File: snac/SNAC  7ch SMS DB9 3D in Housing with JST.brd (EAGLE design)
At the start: 61.2 x 64.1 mm, 51 parts, among them IC1 4030D, IC3 4030D, Q1 BSS138, Q2 BSS138, Q3 BSS138, Q4 BSS138, Q5 BSS138, Q6 BSS138, Q7 BSS138, Q8 BSS138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

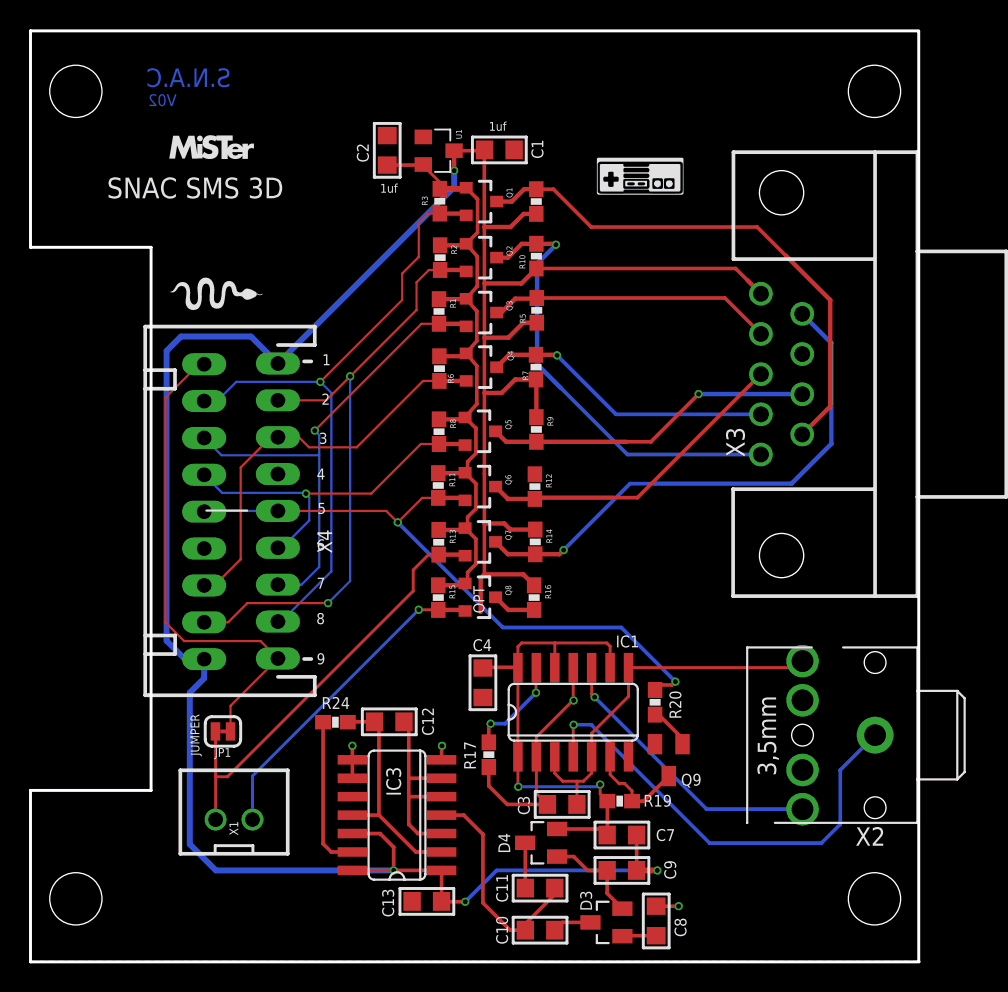
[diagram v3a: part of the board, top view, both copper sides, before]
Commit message: Updated PCB images and README
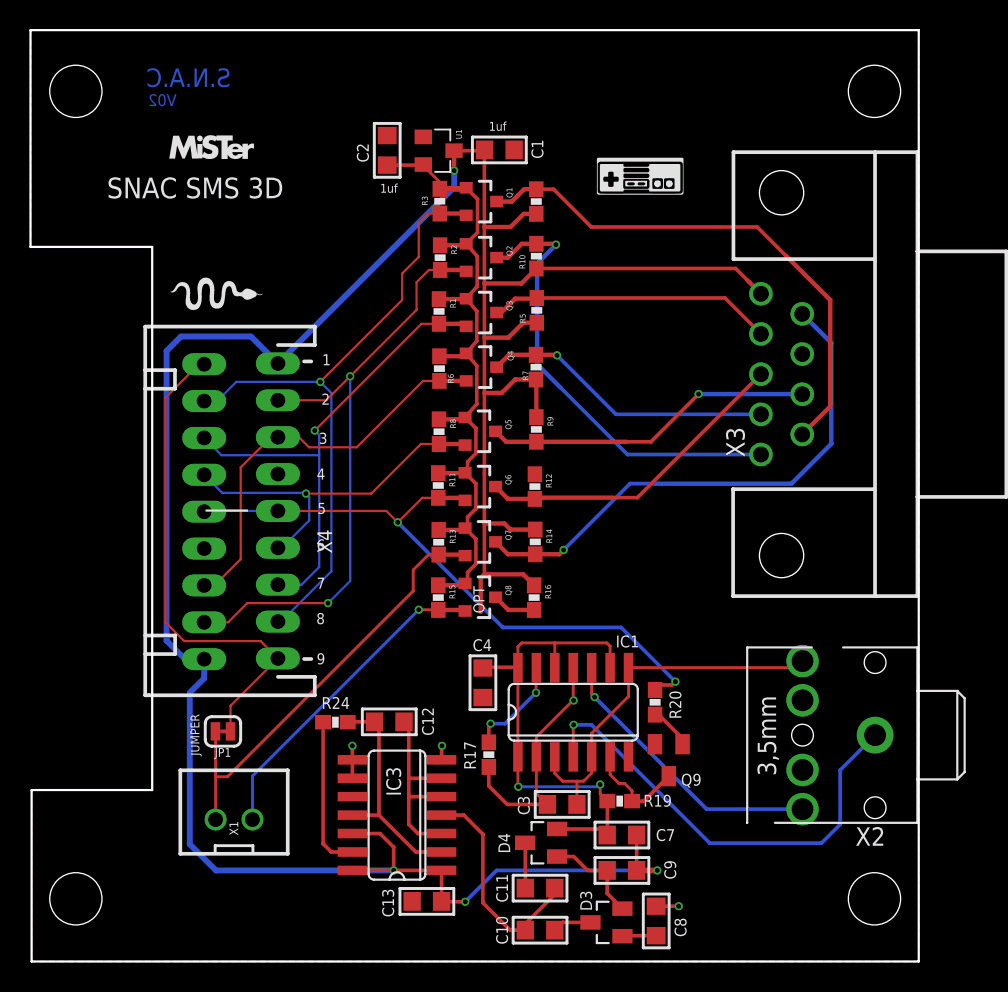
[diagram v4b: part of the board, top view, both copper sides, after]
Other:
- board size 61.2 x 64.1 mm -> 61.2 x 64.2 mm
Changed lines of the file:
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@@
 <text x="12.7" y="15.3162" size="0.6096" layer="21" font="vector" ratio="15" rot="R90">JUMPER</text>
 <text x="6.3246" y="53.721" size="1.4224" layer="21">SNAC SMS 3D</text>
-<wire x1="1.0668" y1="65.2526" x2="1.0668" y2="50.3428" width="0.2032" layer="20"/>
-<wire x1="1.0668" y1="50.3428" x2="9.3726" y2="50.3428" width="0.2032" layer="20"/>
-<wire x1="9.3726" y1="50.3428" x2="9.3726" y2="12.9286" width="0.2032" layer="20"/>
-<wire x1="9.3726" y1="12.9286" x2="1.0668" y2="12.9286" width="0.2032" layer="20"/>
-<wire x1="1.0668" y1="12.9286" x2="1.0668" y2="1.1176" width="0.2032" layer="20"/>
-<wire x1="1.0668" y1="1.1176" x2="62.2808" y2="1.1176" width="0.2032" layer="20"/>
-<wire x1="62.2554" y1="65.2526" x2="1.0668" y2="65.2526" width="0.2032" layer="20"/>
 <rectangle x1="10.67435" y1="47.27575" x2="10.68705" y2="47.28845" layer="21" rot="R270"/>
 <rectangle x1="10.68705" y1="47.27575" x2="10.69975" y2="47.28845" layer="21" rot="R270"/>
@@
 <hole x="4.191" y="5.461" drill="3.6" locked="yes"/>
 <hole x="59.2074" y="5.461" drill="3.6" locked="yes"/>
-<wire x1="62.2554" y1="65.2272" x2="62.2554" y2="1.143" width="0.2032" layer="20"/>
+<wire x1="1.0668" y1="65.3034" x2="62.2554" y2="65.3034" width="0.1524" layer="20"/>
+<wire x1="62.2554" y1="65.3034" x2="62.2554" y2="1.143" width="0.1524" layer="20"/>
+<wire x1="62.2554" y1="1.143" x2="1.143" y2="1.143" width="0.1524" layer="20"/>
+<wire x1="1.143" y1="1.143" x2="1.143" y2="12.954" width="0.1524" layer="20"/>
+<wire x1="1.143" y1="12.954" x2="9.4488" y2="12.954" width="0.1524" layer="20"/>
+<wire x1="9.4488" y1="12.954" x2="9.4488" y2="50.3682" width="0.1524" layer="20"/>
+<wire x1="9.4488" y1="50.3682" x2="1.0668" y2="50.3682" width="0.1524" layer="20"/>
+<wire x1="1.0668" y1="50.3682" x2="1.0668" y2="65.3034" width="0.1524" layer="20"/>
 </plain>
 <attributes>
@@
 <via x="29.4132" y="16.002" extent="1-16" drill="0.3302"/>
 <polygon width="0.2032" layer="1">
-<vertex x="1.0668" y="65.2272"/>
-<vertex x="62.2554" y="65.2272"/>
+<vertex x="1.0668" y="65.3034"/>
+<vertex x="62.2554" y="65.3034"/>
 <vertex x="62.2554" y="1.143"/>
-<vertex x="1.0668" y="1.143"/>
-<vertex x="1.0668" y="12.954"/>
-<vertex x="9.3726" y="12.954"/>
-<vertex x="9.3726" y="50.3682"/>
+<vertex x="1.143" y="1.143"/>
+<vertex x="1.143" y="12.954"/>
+<vertex x="9.4488" y="12.954"/>
+<vertex x="9.4488" y="50.3682"/>
 <vertex x="1.0668" y="50.3682"/>
 </polygon>
 <polygon width="0.2032" layer="16">
-<vertex x="1.0668" y="65.2272"/>
-<vertex x="62.2554" y="65.2272"/>
+<vertex x="1.0668" y="65.3034"/>
+<vertex x="62.2554" y="65.3034"/>
 <vertex x="62.2554" y="1.143"/>
-<vertex x="1.0668" y="1.143"/>
-<vertex x="1.0668" y="12.954"/>
-<vertex x="9.3726" y="12.954"/>
-<vertex x="9.3726" y="50.3682"/>
+<vertex x="1.143" y="1.143"/>
+<vertex x="1.143" y="12.954"/>
+<vertex x="9.4488" y="12.954"/>
+<vertex x="9.4488" y="50.3682"/>
 <vertex x="1.0668" y="50.3682"/>
 </polygon>

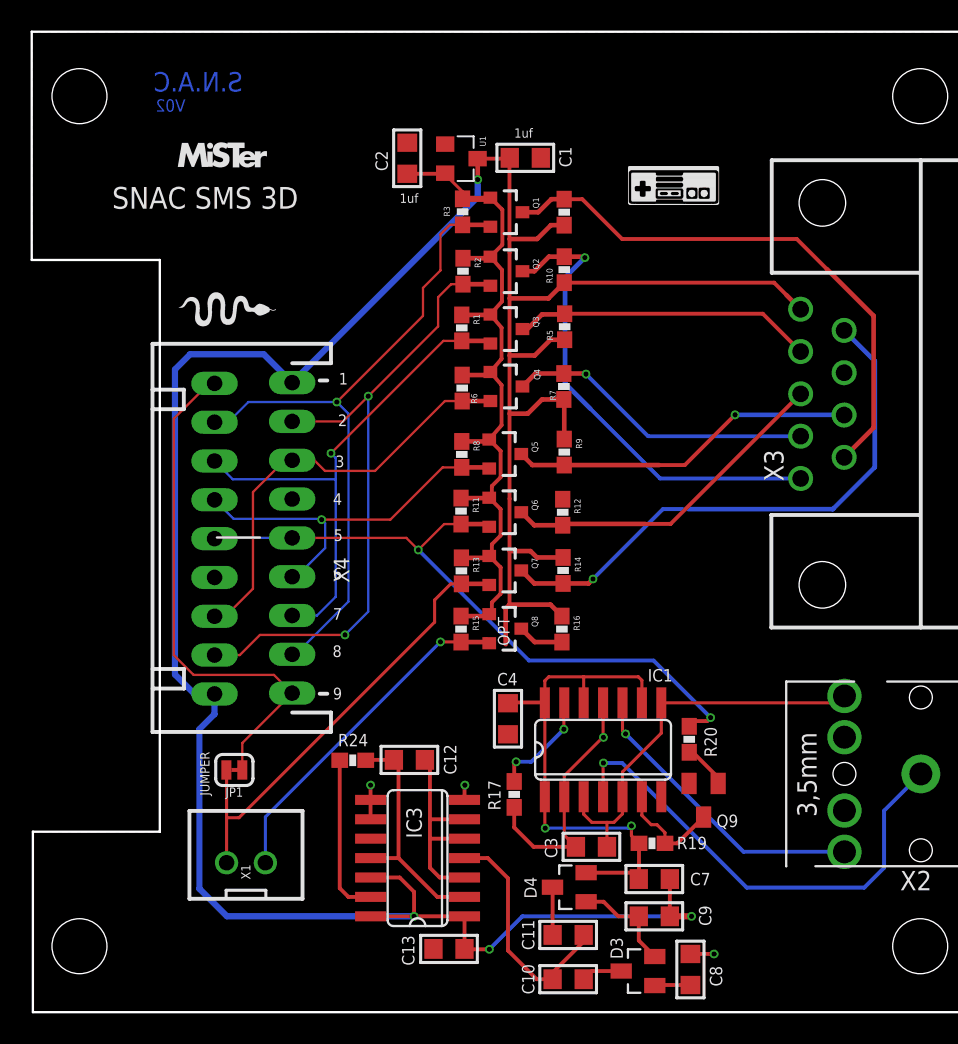
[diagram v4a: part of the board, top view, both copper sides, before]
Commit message: Changed to a MAX660 charge pump on the JST DB9 3D Glasses board
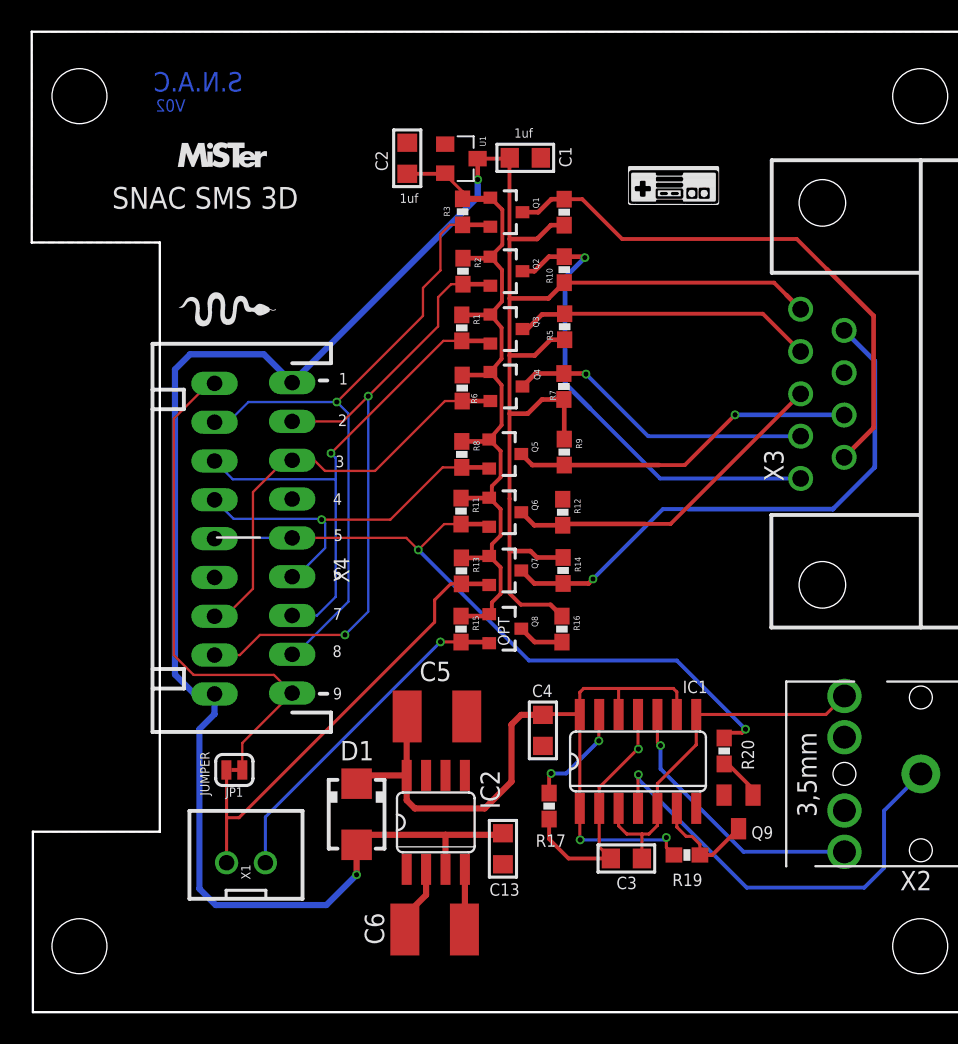
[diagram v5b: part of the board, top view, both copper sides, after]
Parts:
- removed C10, C11, C7, C8, C9: 2.2uF, rc-master-smd:C0805
- removed C12: 10nF, rc-master-smd:C0805
- removed D3, D4: BAS40-04, diode:SOT23
- removed IC3: 4030D, 40xx:SO14
- removed R24: 75K, SparkFun:0603-RES
- added C5, C6: 100uF, rcl:C1812
- added D1: MBRA340T3, diode:SMA
- added IC2: MAX660CPACS, maxim:SO08
- moved C13 7.44 mm to (31.9, 11.8), turned to 270 degrees
- moved C4 2.41 mm to (34.5, 19.6)
- moved IC1 2.41 mm to (40.7, 17.6)
- moved Q9 2.41 mm to (47.3, 14.2)
- moved R19 2.41 mm to (43.9, 11.4)
- moved R20 2.41 mm to (46.4, 18.2)
- moved C3 2.41 mm to (40.0, 11.2)
- moved R17 2.41 mm to (34.9, 14.6)
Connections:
- removed net N$27: C9.1, D3.2, D4.1
- removed net N$28: C8.1, D3.1
- removed net N$29: C11.2, D4.3
- removed net N$30: C10.2, D3.3
- removed net N$31: C12.1, IC3.11, IC3.2, R24.2
- removed net N$32: IC3.13, R24.1
- removed net N$33: C10.1, C11.1, IC3.4
- removed net N$34: C12.2, IC3.3, IC3.5, IC3.6
- new net N$10: C6.1, IC2.2
- new net N$23: C6.2, IC2.4
- net 10V: now also C5.1, D1.C, IC2.8; no longer C7.1, D4.2
- net GND: now also C5.2, IC2.5, IC2.6; no longer C8.2, IC3.7, IC3.8, IC3.9
- net HV: now also D1.A, IC2.3; no longer C7.2, C9.2, IC3.1, IC3.12, IC3.14
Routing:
- net HV: track 188.6 -> 163.6 mm, vias 4 -> 2
- net 10V: track 34.9 -> 51.7 mm
- net N$31: track 15.6 -> 0.00 mm
- net N$33: track 15.6 -> 0.00 mm
- net N$34: track 14.3 -> 0.00 mm
- net N$32: track 10.9 -> 0.00 mm
- net N$27: track 6.91 -> 0.00 mm
- net GND: track 4.76 -> 0.00 mm, vias 3 -> 0
- net N$10: track 0.00 -> 4.51 mm
- net N$23: track 0.00 -> 3.95 mm
- net N$29: track 3.13 -> 0.00 mm
- net N$30: track 2.68 -> 0.00 mm
- net LV6: track 44.4 -> 47.0 mm
- net N$7: track 31.6 -> 29.2 mm
- net N$28: track 2.34 -> 0.00 mm
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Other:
- outline, holes or cut-outs redrawn

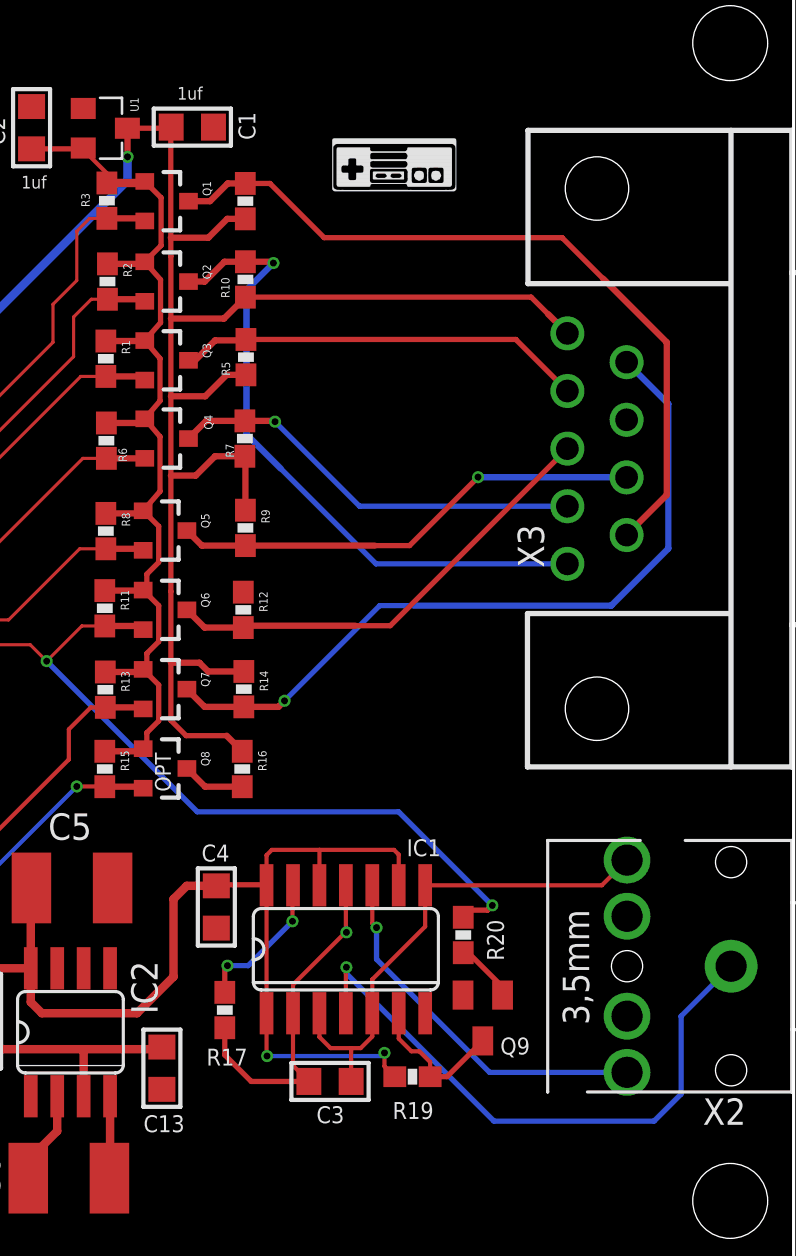
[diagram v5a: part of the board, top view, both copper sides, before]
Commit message: XOR Osc on 3D boards needed an extra resistor
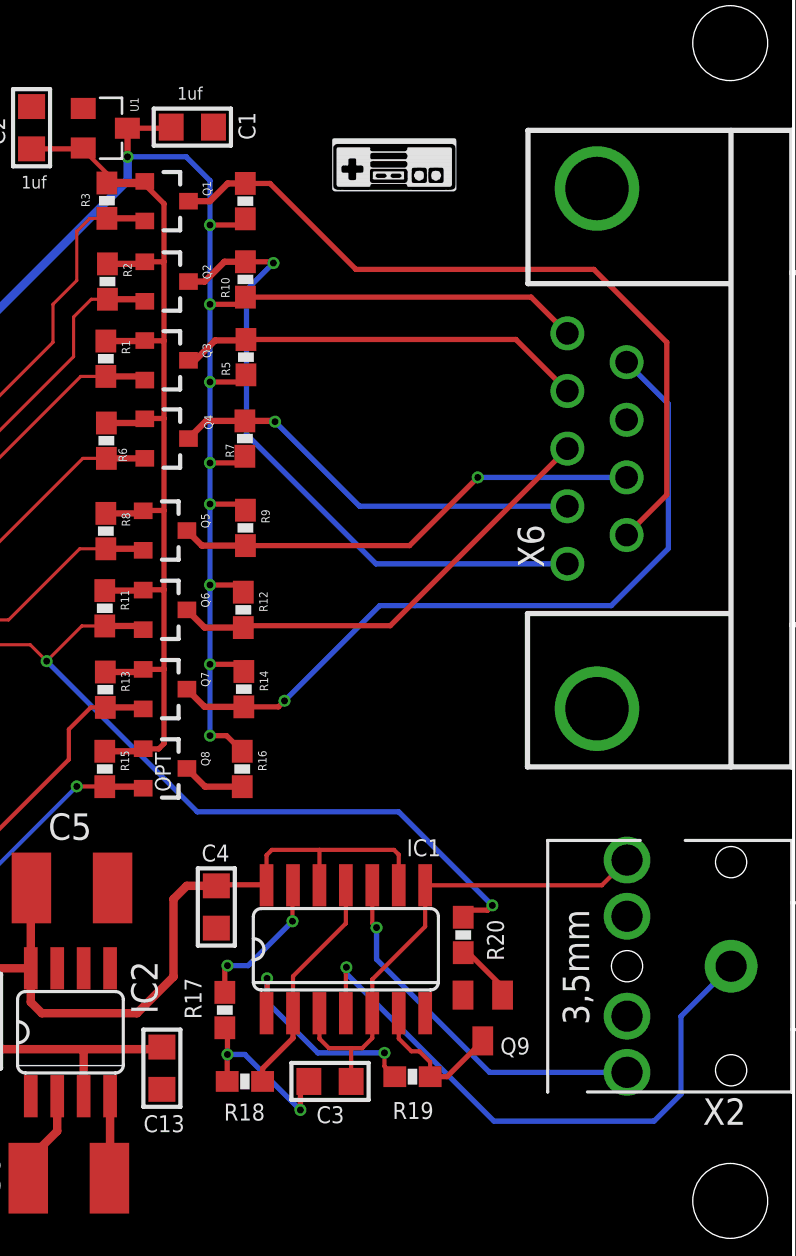
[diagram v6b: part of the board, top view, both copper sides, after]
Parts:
- added R18: 10K, SparkFun:0603-RES
- C3: value 10nF -> 47nF
- renumbered X3 to X6
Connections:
- new net N$24: C3.1, R17.2, R18.1
- net N$5: now also R18.2; no longer C3.1, R17.2
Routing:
- net HV: track 163.6 -> 154.5 mm, vias 2 -> 10
- net N$24: track 0.00 -> 8.79 mm, vias 0 -> 2
- net N$5: track 16.7 -> 11.1 mm, vias 1 -> 0
- net 10V: track 51.7 -> 47.3 mm
- net LV: track 51.8 -> 54.5 mm
